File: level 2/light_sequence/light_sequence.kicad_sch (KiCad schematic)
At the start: 22 parts, among them U1 SA39-11SRWA

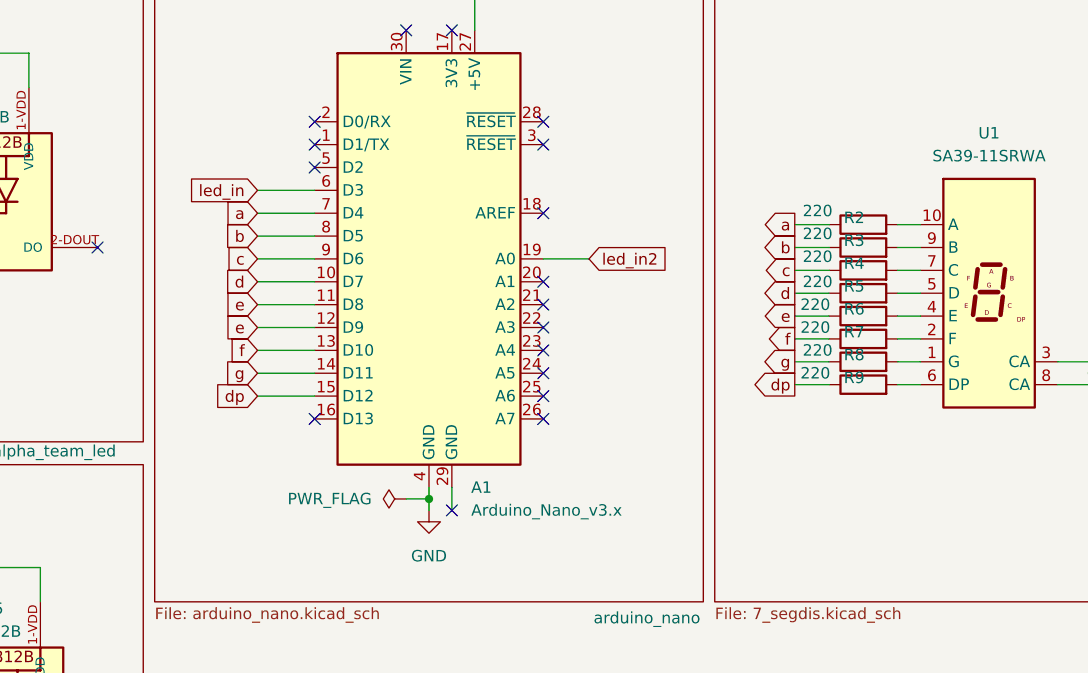
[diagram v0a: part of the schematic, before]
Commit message: light_seq_pcb layout
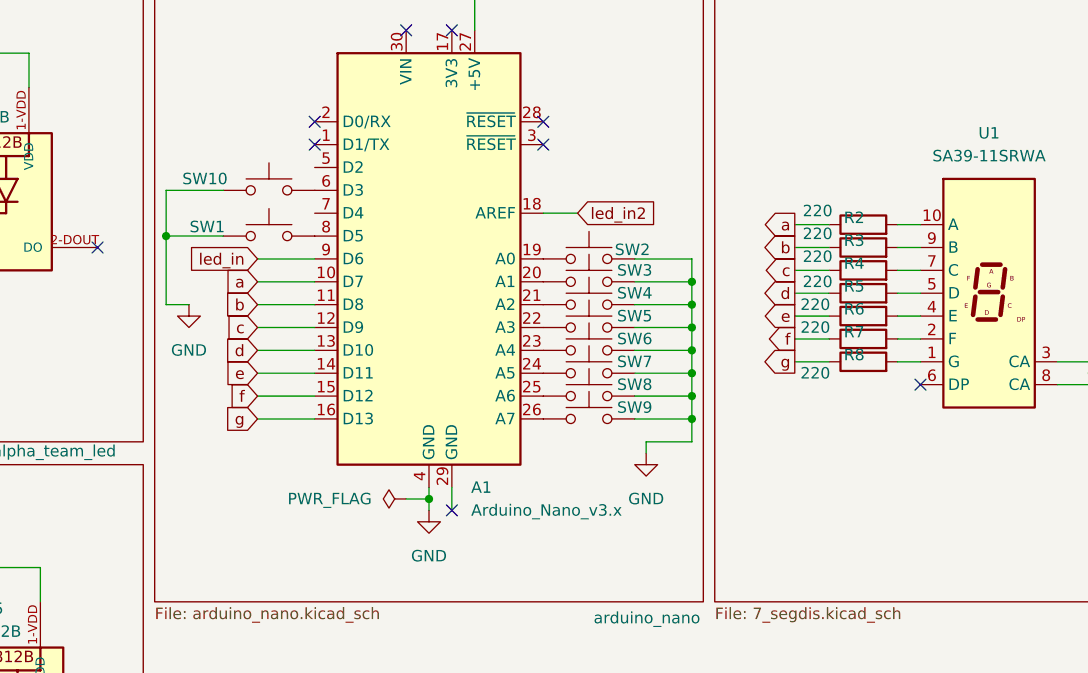
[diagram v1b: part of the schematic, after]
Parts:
- removed R9: 220, Resistor_THT:R_Axial_DIN0207_L6.3mm_D2.5mm_P7.62mm_Horizontal, symbol Device:R
- added SW1, SW10, SW2, SW3, SW4, SW5, SW6, SW7, SW8, SW9: SW_Push, Button_Switch_THT:SW_PUSH_6mm_H7.3mm, symbol Switch:SW_Push
- LED1, LED10, LED2, LED3, LED4, LED5, LED6, LED7, LED8, LED9: footprint (none) -> LED_SMD:LED_WS2812_PLCC6_5.0x5.0mm_P1.6mm
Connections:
- net dp is gone; now on net f: A1.15 (D12)
- net GND: now also SW1.1, SW10.2, SW2.2, SW3.2, SW4.2, SW5.2, SW6.2, SW7.2, SW8.2, SW9.2
- net a: now also A1.10 (D7); no longer A1.7 (D4)
- net b: now also A1.11 (D8); no longer A1.8 (D5)
- net c: now also A1.12 (D9); no longer A1.9 (D6)
- net d: now also A1.13 (D10); no longer A1.10 (D7)
- net e: now also A1.14 (D11); no longer A1.11 (D8), A1.12 (D9)
- net f: no longer A1.13 (D10)
- net g: now also A1.16 (D13); no longer A1.14 (D11)
- net led_in: now also A1.9 (D6); no longer A1.6 (D3)
- net led_in2: now also A1.18 (AREF); no longer A1.19 (A0)
- net at A1.20 (A1): now also SW3.1
- net at A1.21 (A2): now also SW4.1
- net at A1.22 (A3): now also SW5.1
- net at A1.23 (A4): now also SW6.1
- net at A1.24 (A5): now also SW7.1
- net at A1.25 (A6): now also SW8.1
- net at A1.26 (A7): now also SW9.1
- new net: A1.19 (A0), SW2.1
- new net: A1.6 (D3), SW10.1
- new net: A1.8 (D5), SW1.2
- no-connect marks 19 -> 10
